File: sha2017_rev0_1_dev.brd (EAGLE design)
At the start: 65 x 80 mm, 82 parts, among them IC1 CP210X_USB_UART, IC2 AP7215, IC32 ESP32_AI, Q1 MMBT2222A, Q2 MMBT2222A, Q6 MOSFET-NCHANNELBSS123LT1G, SW801 MCMT5-F-V, X701 2908-05WB-MG

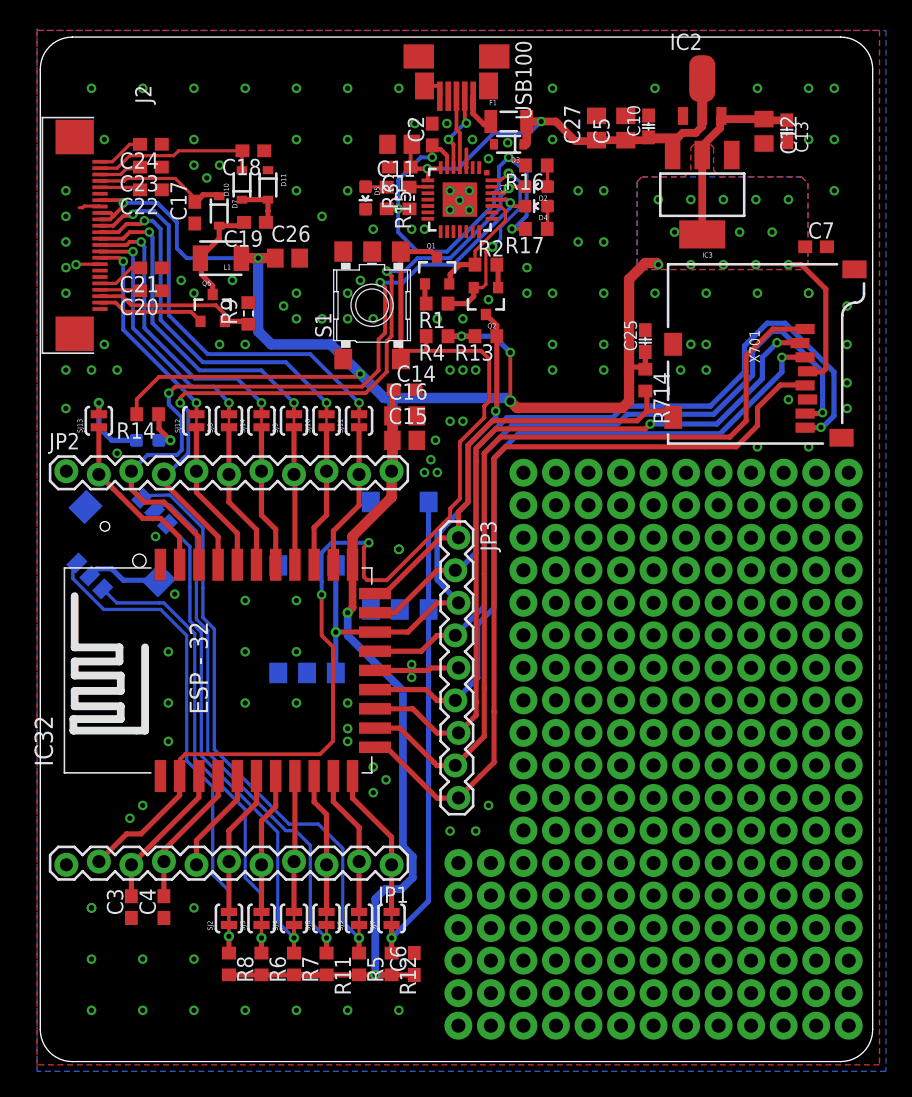
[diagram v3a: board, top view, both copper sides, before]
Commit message: fixed all part designators
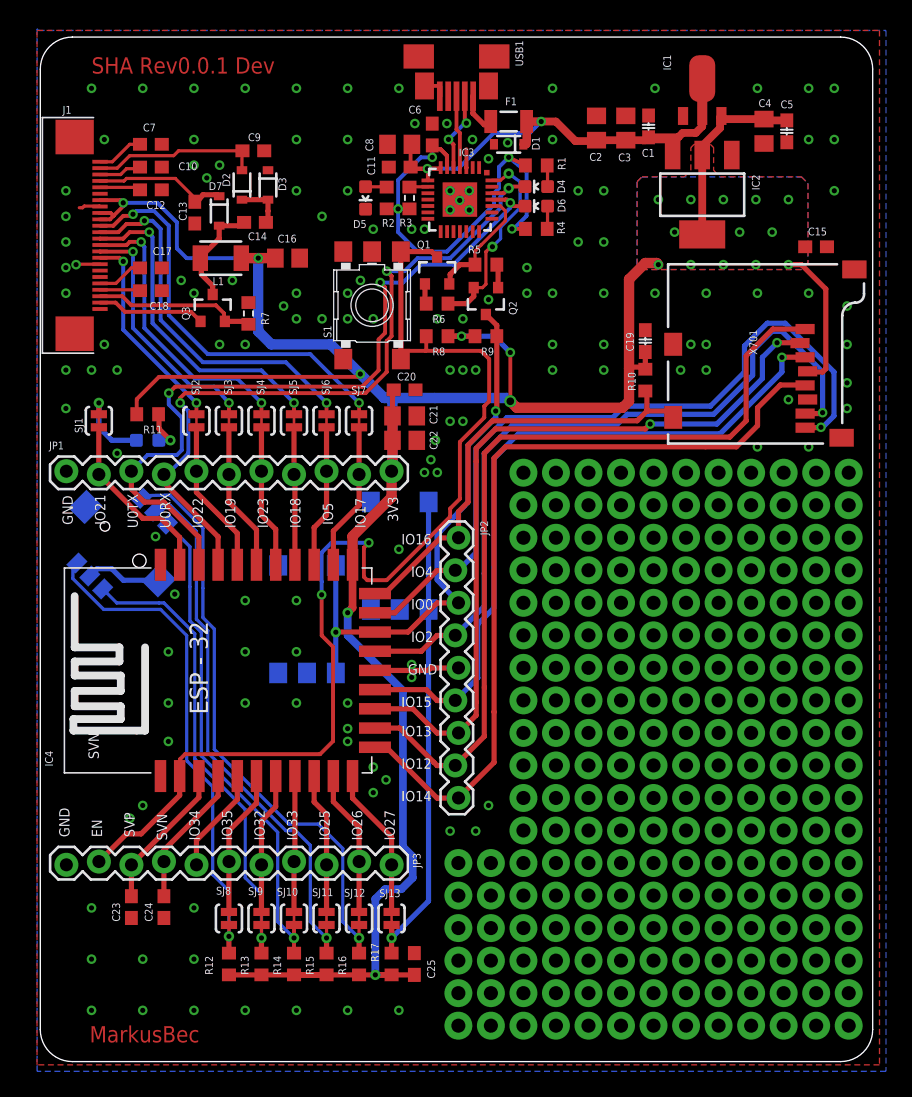
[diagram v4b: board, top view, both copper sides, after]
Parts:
- removed C26: 4u7/16V, rcl:C0805
- removed C27: 2u2/16V, rcl:C0805
- removed D10, D11: NSVR0320MW2T1G, SparkFun-DiscreteSemi:SOD-323
- removed SJ14: JUMPER-PAD-2-NC_BY_TRACE, SparkFun-Passives:PAD-JUMPER-2-NC_BY_TRACE_YES_SILK
- added C8: 100n, rcl:C0805
- added C9: 1u, rcl:C0603
- added D100, D6: (no value), SparkFun-LED:LED-0603
- added SJ1: JUMPER-PAD-2-NC_BY_TRACE, SparkFun-Passives:PAD-JUMPER-2-NC_BY_TRACE_YES_SILK
- C1: value 100n -> 4u7/16V; device rcl:C0603 -> 00ralf:C0603-DASHES
- C10, C13: value 4u7/16V -> 1u; device 00ralf:C0603-DASHES -> rcl:C0603
- C11: device rcl:C0805 -> rcl:C0603
- C12: value 4u7/16V -> 1u; device rcl:C0805 -> rcl:C0603
- C14, C7: value 100n -> 1u
- C15: value 4u7/16V -> 100n; device rcl:C0805 -> rcl:C0603
- C19: device rcl:C0603 -> 00ralf:C0603-DASHES
- C2: value 100n -> 2u2/16V; device rcl:C0603 -> rcl:C0805
- C20: value 1u -> 100n
- C21, C22: value 1u -> 4u7/16V; device rcl:C0603 -> rcl:C0805
- C23, C24: value 1u -> (none)
- C25: value 1u -> 100n; device 00ralf:C0603-DASHES -> rcl:C0603
- C3: value (none) -> 100n; device rcl:C0603 -> rcl:C0805
- C4: value (none) -> 4u7/16V; device rcl:C0603 -> rcl:C0805
- C5: value 100n -> 4u7/16V; device rcl:C0805 -> 00ralf:C0603-DASHES
- D1: value (none) -> PMEG4005EJ; device SparkFun-LED:LED-0603 -> SparkFun-DiscreteSemi:SOD-323
- D2: value (none) -> NSVR0320MW2T1G; device SparkFun-LED:LED-0603 -> SparkFun-DiscreteSemi:SOD-323
- D3: value PMEG4005EJ -> NSVR0320MW2T1G
- IC1: value CP210X_USB_UART -> AP7215; device SparkFun-DigitalIC:MLP28 -> badge:SOT89
- IC2: value AP7215 -> (none); device badge:SOT89 -> SparkFun-PowerIC:SOT223
- IC3: value (none) -> CP210X_USB_UART; device SparkFun-PowerIC:SOT223 -> SparkFun-DigitalIC:MLP28
- JP2: value M11LOCK -> M09LOCK; device SparkFun-Connectors:1X11_LOCK -> SparkFun-Connectors:1X09_LOCK
- JP3: value M09LOCK -> M11LOCK; device SparkFun-Connectors:1X09_LOCK -> SparkFun-Connectors:1X11_LOCK
- R1, R2: value 10K -> (none)
- R11, R4: value 10k -> (none)
- R14, R15, R16, R17: value (none) -> 10k
- R5, R6: value 10k -> 10K
- R7: value 10k -> 5R; device rcl:R0603 -> 00ralf:R0603-DASHES
- R9: value 5R -> 10k; device 00ralf:R0603-DASHES -> rcl:R0603
- moved C4 76.6 mm to (56.5, 72.6), turned to 270 degrees
- moved C3 72.1 mm to (45.7, 72.9)
- moved C6 64.8 mm to (30.6, 72.4)
- moved R16 63.9 mm to (24.9, 7.62), turned to 270 degrees
- moved R15 60.0 mm to (22.4, 7.62)
- moved C24 59.6 mm to (9.65, 12.1), turned to 90 degrees
- moved R17 58.5 mm to (27.4, 7.62), turned to 270 degrees
- moved C23 57.8 mm to (7.11, 12.1), turned to 90 degrees
- moved R5 55.5 mm to (34.8, 62.2), turned to 0 degrees
- moved R6 53.4 mm to (31.0, 59.2), turned to 180 degrees
- moved C7 52.6 mm to (8.64, 71.6), turned to 180 degrees
- moved R13 52.1 mm to (17.3, 7.62), turned to 270 degrees
- moved C25 51.9 mm to (29.2, 7.62)
- moved R8 51.6 mm to (31.0, 56.6), turned to 180 degrees
- moved R7 50.9 mm to (16.3, 58.4), turned to 90 degrees
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- renumbered IC32 to IC4, J2 to J1, Q6 to Q3, R714 to R10, S5 to S101, S6 to S100, SW801 to SW100, USB100 to USB1
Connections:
- net +3V3: now also C19.1, C20.1, C21.1, C22.1, C4.1, C5.1, IC1.3, IC2.2, IC2.4, JP1.11, R15.2, R16.2, R17.2, R8.1, R9.2; no longer C12.1, C13.1, C14.1, C26.1, C6.1, C7.1, IC2.3, IC3.2, IC3.4, JP2.11, R4.1, R5.2, R6.2, R7.2, R8.2
- net +5V: now also C2.1, C3.1, C8.1, D1.C, IC1.2, IC1.2@, IC2.3, IC3.7, IC3.8; no longer C10.1, C27.1, C5.1, D3.C, IC1.7, IC1.8, IC2.2, IC2.2@, IC3.3
- net BT_B: now also R17.1, SJ13.1; no longer R12.1, SJ7.1
- net BT_DOWN: now also R13.1, SJ9.1; no longer R6.1, SJ3.1
- net BT_LEFT: now also R14.1, SJ10.1; no longer R7.1, SJ4.1
- net BT_MID: now also R15.1, SJ11.1; no longer R11.1, SJ6.1
- net BT_RIGHT: now also R12.1, SJ8.1; no longer R8.1, SJ2.1
- net BT_UP: now also R16.1, SJ12.1; no longer R5.1, SJ5.1
- net ESP32_!RESET: now also JP3.10, R8.2; no longer JP1.10, R4.2
- net ESP32_FLASH/TOUCHE_MENU: now also JP2.3, R9.1; no longer JP3.3, R13.1
- net ESP32_RX: now also D4.C, IC3.26, JP1.4; no longer D2.C, IC1.26, JP2.4
- net ESP32_TX: now also D6.C, IC3.25, JP1.3; no longer D4.C, IC1.25, JP2.3
- net GND: now also C10.1, C12.1, C13.1, C19.2, C20.2, C21.2, C22.2, C3.2, C4.2, C7.1, C8.2, C9.1, D1.A, D3.C, IC1.1, IC3.3, IC3.EXP, IC3.M, JP1.1, JP2.5, JP3.11, R7.2; no longer C10.2, C12.2, C13.2, C14.2, C20.1, C21.1, C22.1, C26.2, C27.2, C3.1, C4.1, C7.2, D11.C, D3.A, IC1.3, IC1.EXP, IC1.M, IC3.1, JP1.11, JP2.1, JP3.5, R9.2
- net LCD_!RESET: now also SJ3.2; no longer SJ8.2
- net LCD_BUSY: now also SJ2.2; no longer SJ12.2
- net LCD_CS: now also SJ5.2; no longer SJ9.2
- net LCD_D/!S: now also SJ4.2; no longer SJ14.2
- net LCD_MOSI: now also SJ7.2; no longer SJ11.2
- net LCD_SCK: now also SJ6.2; no longer SJ10.2
- net LED1: now also D100.C, SJ1.2; no longer D1.C, SJ13.2
- net N$1: now also C23.2, JP3.9; no longer C3.2, JP1.9
- net N$10: now also IC3.24, R5.1; no longer IC1.24, R2.1
- net N$11: now also IC3.28, R6.1; no longer IC1.28, R1.1
- net N$12: now also JP3.6, SJ8.2; no longer JP1.6, SJ2.2
- net N$13: now also R5.2; no longer R2.2
- net N$14: now also R6.2; no longer R1.2
- net N$15: now also JP3.7; no longer JP1.7
- net N$16: now also JP1.2, SJ1.1; no longer JP2.2, SJ13.1
- net N$17: now also JP1.5, SJ2.1; no longer JP2.5, SJ12.1
- net N$18: now also JP1.7, SJ4.1; no longer JP2.7, SJ14.1
- net N$19: now also JP1.6, SJ3.1; no longer JP2.6, SJ8.1
- net N$2: now also C24.2, JP3.8; no longer C4.2, JP1.8
- net N$20: now also JP1.8, SJ5.1; no longer JP2.8, SJ9.1
- net N$21: now also JP1.9, SJ6.1; no longer JP2.9, SJ10.1
- net N$22: now also C14.1, D2.C, D3.A; no longer C19.1, D10.C, D11.A
- net N$23: now also C14.2; no longer C19.2
- net N$24: now also JP1.10, SJ7.1; no longer JP2.10, SJ11.1
- net N$25: now also D100.A, R11.1; no longer D1.A, R14.1
- net N$26: now also R2.1; no longer R15.1
- net N$27: now also D4.A, R1.1; no longer D2.A, R16.1
- net N$28: now also D6.A, R4.1; no longer D4.A, R17.1
- net N$3: now also JP3.1, SJ13.2; no longer JP1.1, SJ7.2
- net N$4: now also JP3.2, SJ12.2; no longer JP1.2, SJ5.2
- net N$6: now also JP3.3, SJ11.2; no longer JP1.3, SJ6.2
- net N$7: now also JP3.4, SJ10.2; no longer JP1.4, SJ4.2
- net N$8: now also IC3.9; no longer IC1.9
- net N$9: now also JP3.5, SJ9.2; no longer JP1.5, SJ3.2
- net PREVGH: now also C13.2; no longer C17.2
- net PREVGL: now also C9.2, D2.A; no longer C18.2, D10.A
- net RESE: now also R7.1; no longer R9.1
- net SD_CD: now also JP2.1; no longer JP3.1
- net SD_CLK: now also JP2.9; no longer JP3.9
- net SD_CMD: now also JP2.6; no longer JP3.6
- net SD_DATA0: now also JP2.4; no longer JP3.4
- net SD_DATA1: now also JP2.2; no longer JP3.2
- net SD_DATA2: now also JP2.8; no longer JP3.8
- net SD_DATA3: now also JP2.7; no longer JP3.7
- net USB_DN_CON: now also IC3.5; no longer IC1.5
- net USB_DP_CON: now also IC3.4; no longer IC1.4
- net VCOM: now also C7.2; no longer C24.2
- net VDD: now also C6.1, IC3.6, R1.2, R2.2, R4.2; no longer C2.1, IC1.6, R15.2, R16.2, R17.2
- net VGH: now also C17.2; no longer C21.2
- net VGL: now also C18.2; no longer C20.2
- net VSH: now also C12.2; no longer C22.2
- net VSL: now also C10.2; no longer C23.2
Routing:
- net GND: vias 143 -> 140
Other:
- board text added: "3V3"
- board text added: "EN"
- board text added: "GND"
- board text added: "IO0"
- board text added: "IO12"
- board text added: "IO13"
- board text added: "IO14"
- board text added: "IO15"
- board text added: "IO16"
- board text added: "IO17"
- board text added: "IO18"
- board text added: "IO19"
- board text added: "IO2"
- board text added: "IO21"
- board text added: "IO22"
- board text added: "IO23"
- board text added: "IO25"
- board text added: "IO26"
- board text added: "IO27"
- board text added: "IO32"
- board text added: "IO33"
- board text added: "IO34"
- board text added: "IO35"
- board text added: "IO4"
- board text added: "IO5"
- board text added: "MarkusBec"
- board text added: "SHA Rev0.0.1 Dev"
- board text added: "SVN"
- board text added: "SVP"
- board text added: "U0RX"
- board text added: "U0TX"

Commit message: some PCB tweeking
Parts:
- added FD1, FD2, FD3, FD4, FD5: FIDUCIAL, adafruit:FIDUCIAL_1MM
- D1: value PMEG4005EJ -> SD05-7
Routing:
- net GND: vias 140 -> 149
- net +5V: vias 2 -> 18
- added copper zone on layer 1, net +5V
- added copper zone on layer 16, net +5V

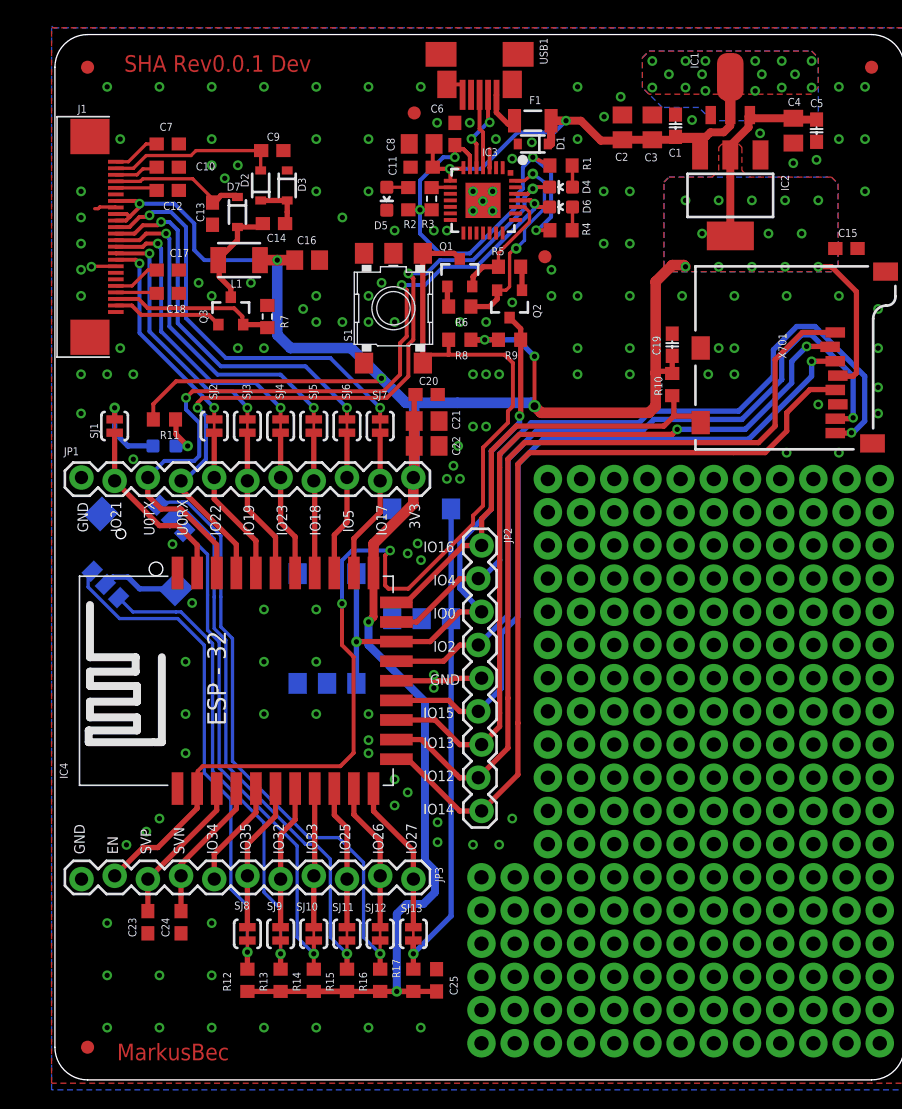
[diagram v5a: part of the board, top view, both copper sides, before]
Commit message: changed ESP module to WROOM32
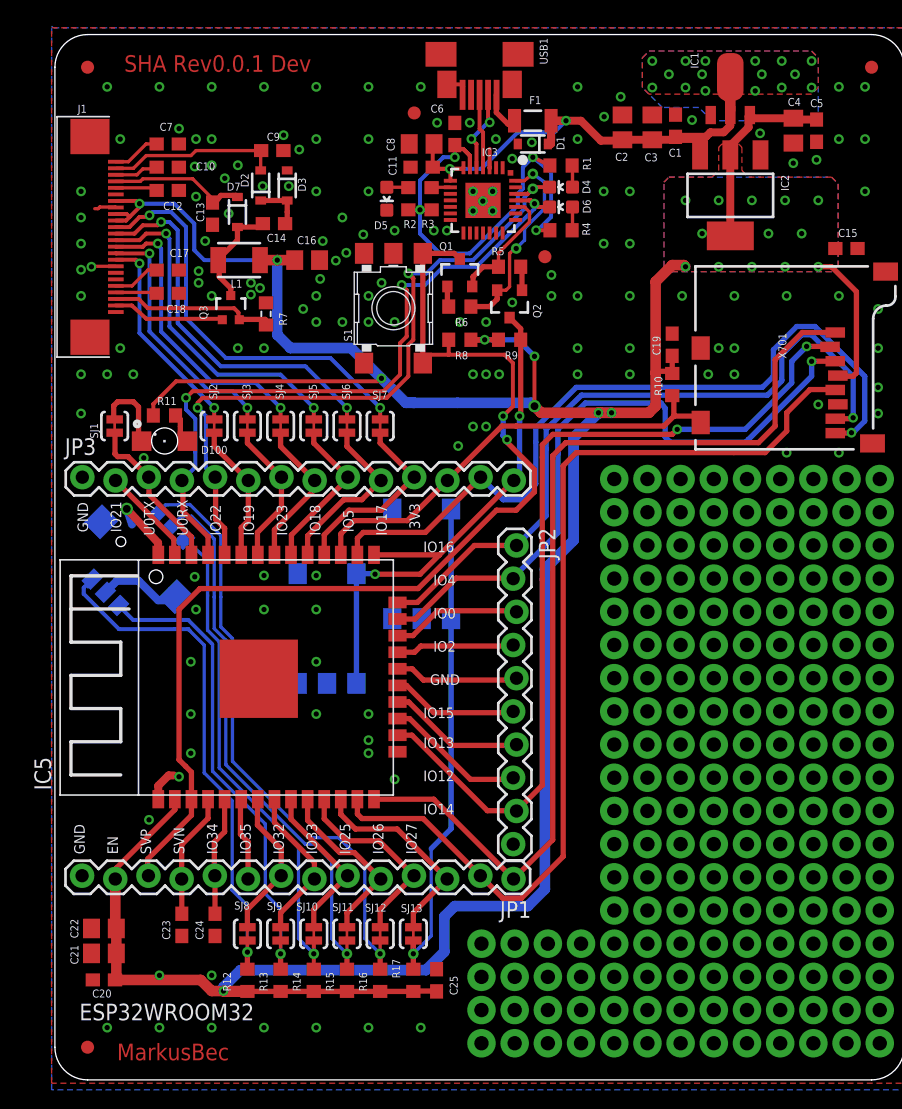
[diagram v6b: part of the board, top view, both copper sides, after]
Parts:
- removed IC4: ESP32_AI, badge:ESP32_AI
- added IC5: ESP32WROOM32, ESP3x:ESP32MOD
- C1, C5: value 4u7/16V -> 100n; device 00ralf:C0603-DASHES -> rcl:C0603
- C19: device 00ralf:C0603-DASHES -> rcl:C0603
- C2: value 2u2/16V -> 4u7/16V
- C3, C8: value 100n -> 4u7/16V
- D100: value (none) -> Green; device SparkFun-LED:LED-0603 -> led:SML1206
- D4: value (none) -> Yellow
- D5: value (none) -> green
- D6: value (none) -> RED
- IC2: value (none) -> LM1117
- JP1, JP3: value M11LOCK -> M14LOCK; device SparkFun-Connectors:1X11_LOCK -> SparkFun-Connectors:1X14_LOCK
- JP2: value M09LOCK -> M10LOCK; device SparkFun-Connectors:1X09_LOCK -> SparkFun-Connectors:1X10_LOCK
- Q3: value MOSFET-NCHANNELBSS123LT1G -> SI1304 BDL; device SparkFun-DiscreteSemi:SOT23-3 -> SparkFun-DiscreteSemi:SOT323
- R1, R11, R2, R4: value (none) -> 1k
- R3: device 00ralf:R0603-DASHES -> rcl:R0603
- R5, R6: value 10K -> 10k
- moved C20 51.2 mm to (3.75, 7.65), turned to 180 degrees
- moved C21 47.6 mm to (3.75, 9.68), turned to 180 degrees
- moved JP1 45.0 mm to (35.1, 15.5), turned to 180 degrees
- moved C22 44.4 mm to (3.75, 11.6), turned to 180 degrees
- moved JP3 39.7 mm to (2.10, 46.0), turned to 0 degrees
- moved JP2 2.67 mm to (35.2, 40.9)
- moved C24 2.61 mm to (12.3, 11.9)
- moved C23 2.61 mm to (9.71, 11.9)
- moved SW100 0.60 mm to (6.39, 39.8)
- moved D100 0.37 mm to (8.39, 48.9), flipped to the top, turned to 0 degrees
- moved Q3 0.30 mm to (13.5, 59.1)
- moved R11 0.30 mm to (8.38, 50.8)
- moved R7 0.22 mm to (16.2, 58.6)
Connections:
- removed net N$19: IC4.26, JP1.6, SJ3.1
- removed net N$2: C24.2, IC4.4, JP3.8
- new net N$42: C23.2, IC5.4, JP1.11
- new net N$43: C24.2, IC5.5, JP1.10
- new net N$44: IC5.7, JP1.8, SJ8.2
- new net N$45: IC5.8, JP1.7, SJ9.2
- new net N$46: IC5.9, JP1.6, SJ10.2
- new net N$47: IC5.10, JP1.5, SJ11.2
- new net N$48: IC5.11, JP1.4, SJ12.2
- new net N$49: IC5.12, JP1.3, SJ13.2
- new net N$63: IC5.31, JP3.8, SJ4.1
- net +3V3: now also IC5.2, JP1.13; no longer IC4.21, JP1.11
- net ESP32_!RESET: now also IC5.3, JP1.12; no longer IC4.2, JP3.10
- net ESP32_FLASH/TOUCHE_MENU: now also IC5.25, JP3.14; no longer IC4.18, JP2.3
- net ESP32_RX: now also IC5.34, JP3.5; no longer IC4.28, JP1.4
- net ESP32_TX: now also IC5.35, JP3.4; no longer IC4.29, JP1.3
- net GND: now also IC5.0, IC5.1, IC5.15, IC5.38, JP1.14, JP2.10, JP3.1; no longer IC4.1, IC4.16, IC4.31, JP1.1, JP2.5, JP3.11
- net N$1: now also IC5.6, JP1.9; no longer C23.2, IC4.3, JP3.9
- net N$12: now also IC5.22, JP2.3; no longer IC4.6, JP3.6, SJ8.2
- net N$15: now also IC5.37, JP3.2; no longer IC4.5, JP3.7
- net N$16: now also IC5.36, JP3.3; no longer IC4.30, JP1.2
- net N$17: now also IC5.33, JP3.6; no longer IC4.27, JP1.5
- net N$18: now also IC5.32, JP3.7, SJ3.1; no longer IC4.25, JP1.7, SJ4.1
- net N$20: now also IC5.30, JP3.9; no longer IC4.24, JP1.8
- net N$21: now also IC5.29, JP3.10; no longer IC4.23, JP1.9
- net N$24: now also IC5.28, JP3.11; no longer IC4.22, JP1.10
- net N$3: now also IC5.17, JP2.8; no longer IC4.11, JP3.1, SJ13.2
- net N$4: now also IC5.18, JP2.7; no longer IC4.10, JP3.2, SJ12.2
- net N$6: now also IC5.19, JP2.6; no longer IC4.9, JP3.3, SJ11.2
- net N$7: now also IC5.20, JP2.5; no longer IC4.8, JP3.4, SJ10.2
- net N$9: now also IC5.21, JP2.4; no longer IC4.7, JP3.5, SJ9.2
- net SD_CD: now also IC5.27, JP3.12; no longer IC4.20, JP2.1
- net SD_CLK: now also IC5.13, JP1.2; no longer IC4.12, JP2.9
- net SD_CMD: now also IC5.23, JP2.2; no longer IC4.15, JP2.6
- net SD_DATA0: now also IC5.24, JP2.1; no longer IC4.17, JP2.4
- net SD_DATA1: now also IC5.26, JP3.13; no longer IC4.19, JP2.2
- net SD_DATA2: now also IC5.14, JP1.1; no longer IC4.13, JP2.8
- net SD_DATA3: now also IC5.16, JP2.9; no longer IC4.14, JP2.7
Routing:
- net +3V3: track 208.7 -> 244.8 mm, vias 21 -> 22
- net N$49: track 0.00 -> 16.1 mm
- net N$48: track 0.00 -> 15.2 mm
- net N$47: track 0.00 -> 13.8 mm
- net N$46: track 0.00 -> 12.7 mm
- net N$45: track 0.00 -> 12.1 mm
- net N$63: track 0.00 -> 11.7 mm
- net N$44: track 0.00 -> 11.6 mm
- net N$19: track 11.6 -> 0.00 mm
- net SD_CLK: track 63.3 -> 74.8 mm
- net N$2: track 11.1 -> 0.00 mm
- net SD_DATA2: track 64.8 -> 75.4 mm
- net N$42: track 0.00 -> 9.61 mm
- net N$43: track 0.00 -> 9.17 mm
- net SD_DATA3: track 59.8 -> 66.5 mm
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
